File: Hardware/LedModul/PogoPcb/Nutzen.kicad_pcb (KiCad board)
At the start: 2 copper layers, 96 x 96 mm, 150 parts, among them J1 Conn_01x01_Pin, J2 Conn_01x01_Pin, J3 Conn_01x01_Pin, J4 Conn_01x01_Pin, J5 Conn_01x01_Pin, J6 Conn_01x01_Pin

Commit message: added gerber data
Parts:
- removed the J1 at (80.4, 98.5)
- removed the J1 at (99.6, 79.3)
- removed the J1 at (157.2, 79.3)
- removed the J1 at (138.0, 79.3)
- removed the J1 at (99.6, 60.1)
- removed the J1 at (138.0, 98.5)
- removed the J1 at (80.4, 79.3)
- removed the J1 at (118.8, 60.1)
- removed the J1 at (138.0, 136.9)
- removed the J1 at (99.6, 136.9)
- removed the J1 at (157.2, 60.1)
- removed the J1 at (99.6, 117.7)
- removed the J1 at (138.0, 60.1)
- removed the J1 at (118.8, 79.3)
- removed the J1 at (99.6, 98.5)
- removed the J1 at (80.4, 136.9)
- removed the J1 at (157.2, 117.7)
- removed the J1 at (138.0, 117.7)
- removed the J1 at (157.2, 136.9)
- removed the J1 at (80.4, 117.7)
- removed the J1 at (157.2, 98.5)
- removed the J1 at (118.8, 117.7)
- removed the J1 at (80.4, 60.1)
- removed the J1 at (118.8, 136.9)
- removed the J1 at (118.8, 98.5)
- removed the J2 at (102.8, 115.4)
- removed the J2 at (122.0, 115.4)
- removed the J2 at (83.6, 115.4)
- removed the J2 at (160.4, 134.6)
- removed the J2 at (160.4, 57.8)
- removed the J2 at (102.8, 96.2)
- removed the J2 at (102.8, 134.6)
- removed the J2 at (141.2, 134.6)
- removed the J2 at (141.2, 57.8)
- removed the J2 at (102.8, 57.8)
- removed the J2 at (141.2, 115.4)
- removed the J2 at (102.8, 77.0)
- removed the J2 at (122.0, 96.2)
- removed the J2 at (83.6, 77.0)
- removed the J2 at (141.2, 77.0)
- removed the J2 at (160.4, 96.2)
- removed the J2 at (122.0, 57.8)
- removed the J2 at (141.2, 96.2)
- removed the J2 at (122.0, 77.0)
- removed the J2 at (160.4, 115.4)
- removed the J2 at (122.0, 134.6)
- removed the J2 at (160.4, 77.0)
- removed the J2 at (83.6, 96.2)
- removed the J2 at (83.6, 134.6)
- removed the J2 at (83.6, 57.8)
- removed the J3 at (73.2, 77.0)
- removed the J3 at (73.2, 134.6)
- removed the J3 at (92.4, 77.0)
- removed the J3 at (92.4, 57.8)
- removed the J3 at (73.2, 57.8)
- removed the J3 at (150.0, 96.2)
- removed the J3 at (73.2, 96.2)
- removed the J3 at (130.8, 77.0)
- removed the J3 at (130.8, 57.8)
- removed the J3 at (111.6, 115.4)
- removed the J3 at (92.4, 96.2)
- removed the J3 at (111.6, 96.2)
- removed the J3 at (111.6, 134.6)
- removed the J3 at (130.8, 134.6)
- removed the J3 at (111.6, 57.8)
- removed the J3 at (150.0, 134.6)
- removed the J3 at (73.2, 115.4)
- removed the J3 at (150.0, 77.0)
- removed the J3 at (111.6, 77.0)
- removed the J3 at (150.0, 57.8)
- removed the J3 at (92.4, 134.6)
- removed the J3 at (92.4, 115.4)
- removed the J3 at (150.0, 115.4)
- removed the J3 at (130.8, 115.4)
- removed the J3 at (130.8, 96.2)
- removed the J4 at (134.0, 117.7)
- removed the J4 at (114.8, 98.5)
- removed the J4 at (114.8, 136.9)
- removed the J4 at (114.8, 117.7)
- removed the J4 at (76.4, 98.5)
- removed the J4 at (95.6, 98.5)
- removed the J4 at (76.4, 136.9)
- removed the J4 at (153.2, 60.1)
- removed the J4 at (114.8, 79.3)
- removed the J4 at (114.8, 60.1)
- removed the J4 at (76.4, 60.1)
- removed the J4 at (95.6, 136.9)
- removed the J4 at (134.0, 98.5)
- removed the J4 at (95.6, 79.3)
- removed the J4 at (134.0, 136.9)
- removed the J4 at (153.2, 98.5)
- removed the J4 at (95.6, 60.1)
- removed the J4 at (153.2, 136.9)
- removed the J4 at (134.0, 79.3)
- removed the J4 at (76.4, 79.3)
- removed the J4 at (95.6, 117.7)
- removed the J4 at (76.4, 117.7)
- removed the J4 at (134.0, 60.1)
- removed the J4 at (153.2, 117.7)
- removed the J4 at (153.2, 79.3)
- removed the J5 at (155.2, 68.0)
- removed the J5 at (78.4, 106.4)
- removed the J5 at (97.6, 87.2)
- removed the J5 at (78.4, 68.0)
- removed the J5 at (136.0, 87.2)
- removed the J5 at (136.0, 48.8)
- removed the J5 at (155.2, 125.6)
- removed the J5 at (116.8, 106.4)
- removed the J5 at (155.2, 48.8)
- removed the J5 at (116.8, 68.0)
- removed the J5 at (116.8, 125.6)
- removed the J5 at (97.6, 125.6)
- removed the J5 at (116.8, 87.2)
- removed the J5 at (136.0, 125.6)
- removed the J5 at (97.6, 106.4)
- removed the J5 at (78.4, 48.8)
- removed the J5 at (136.0, 68.0)
- removed the J5 at (78.4, 87.2)
- removed the J5 at (97.6, 68.0)
- removed the J5 at (155.2, 106.4)
- removed the J5 at (136.0, 106.4)
- removed the J5 at (155.2, 87.2)
- removed the J5 at (116.8, 48.8)
- removed the J5 at (97.6, 48.8)
- removed the J5 at (78.4, 125.6)
- removed the J6 at (97.6, 136.9)
- removed the J6 at (97.6, 60.1)
- removed the J6 at (116.8, 79.3)
- removed the J6 at (155.2, 117.7)
- removed the J6 at (78.4, 98.5)
- removed the J6 at (78.4, 79.3)
- removed the J6 at (78.4, 117.7)
- removed the J6 at (136.0, 79.3)
- removed the J6 at (97.6, 98.5)
- removed the J6 at (116.8, 98.5)
- removed the J6 at (155.2, 79.3)
- removed the J6 at (136.0, 136.9)
- removed the J6 at (136.0, 60.1)
- removed the J6 at (97.6, 117.7)
- removed the J6 at (78.4, 60.1)
- removed the J6 at (97.6, 79.3)
- removed the J6 at (155.2, 60.1)
- removed the J6 at (116.8, 117.7)
- removed the J6 at (155.2, 98.5)
- removed the J6 at (155.2, 136.9)
- removed the J6 at (78.4, 136.9)
- removed the J6 at (116.8, 136.9)
- removed the J6 at (136.0, 98.5)
- removed the J6 at (136.0, 117.7)
- removed the J6 at (116.8, 60.1)
- added J1: Conn_01x01_Pin, Bergi:Solderpad_1x2, B.Cu at (114.0, 88.8)
- added J1: Conn_01x01_Pin, Bergi:Solderpad_1x2, B.Cu at (190.8, 88.8)
- added J1: Conn_01x01_Pin, Bergi:Solderpad_1x2, B.Cu at (171.7, 108.0)
- added J1: Conn_01x01_Pin, Bergi:Solderpad_1x2, B.Cu at (133.2, 50.4)
- added J1: Conn_01x01_Pin, Bergi:Solderpad_1x2, B.Cu at (133.2, 127.2)
- added J1: Conn_01x01_Pin, Bergi:Solderpad_1x2, B.Cu at (190.8, 50.4)
- added J1: Conn_01x01_Pin, Bergi:Solderpad_1x2, B.Cu at (171.7, 50.4)
- added J1: Conn_01x01_Pin, Bergi:Solderpad_1x2, B.Cu at (152.4, 88.8)
- added J1: Conn_01x01_Pin, Bergi:Solderpad_1x2, B.Cu at (114.0, 69.6)
- added J1: Conn_01x01_Pin, Bergi:Solderpad_1x2, B.Cu at (190.8, 127.2)
- added J1: Conn_01x01_Pin, Bergi:Solderpad_1x2, B.Cu at (152.4, 127.2)
- added J1: Conn_01x01_Pin, Bergi:Solderpad_1x2, B.Cu at (133.2, 108.0)
- added J1: Conn_01x01_Pin, Bergi:Solderpad_1x2, B.Cu at (114.0, 127.2)
- added J1: Conn_01x01_Pin, Bergi:Solderpad_1x2, B.Cu at (114.0, 108.0)
- added J1: Conn_01x01_Pin, Bergi:Solderpad_1x2, B.Cu at (152.4, 50.4)
- added J1: Conn_01x01_Pin, Bergi:Solderpad_1x2, B.Cu at (133.2, 88.8)
- added J1: Conn_01x01_Pin, Bergi:Solderpad_1x2, B.Cu at (171.7, 127.2)
- added J1: Conn_01x01_Pin, Bergi:Solderpad_1x2, B.Cu at (152.4, 108.0)
- added J1: Conn_01x01_Pin, Bergi:Solderpad_1x2, B.Cu at (171.7, 88.8)
- added J1: Conn_01x01_Pin, Bergi:Solderpad_1x2, B.Cu at (171.7, 69.6)
- added J1: Conn_01x01_Pin, Bergi:Solderpad_1x2, B.Cu at (133.2, 69.6)
- added J1: Conn_01x01_Pin, Bergi:Solderpad_1x2, B.Cu at (114.0, 50.4)
- added J1: Conn_01x01_Pin, Bergi:Solderpad_1x2, B.Cu at (152.4, 69.6)
- added J1: Conn_01x01_Pin, Bergi:Solderpad_1x2, B.Cu at (190.8, 108.0)
- added J1: Conn_01x01_Pin, Bergi:Solderpad_1x2, B.Cu at (190.8, 69.6)
- added J2: Conn_01x01_Pin, TestPoint:TestPoint_Pad_D2.0mm, F.Cu at (136.4, 67.3)
- added J2: Conn_01x01_Pin, TestPoint:TestPoint_Pad_D2.0mm, F.Cu at (194.1, 48.1)
- added J2: Conn_01x01_Pin, TestPoint:TestPoint_Pad_D2.0mm, F.Cu at (194.1, 86.5)
- added J2: Conn_01x01_Pin, TestPoint:TestPoint_Pad_D2.0mm, F.Cu at (155.7, 48.1)
- added J2: Conn_01x01_Pin, TestPoint:TestPoint_Pad_D2.0mm, F.Cu at (117.2, 67.3)
- added J2: Conn_01x01_Pin, TestPoint:TestPoint_Pad_D2.0mm, F.Cu at (155.7, 86.5)
- added J2: Conn_01x01_Pin, TestPoint:TestPoint_Pad_D2.0mm, F.Cu at (174.8, 86.5)
- added J2: Conn_01x01_Pin, TestPoint:TestPoint_Pad_D2.0mm, F.Cu at (155.7, 105.7)
- added J2: Conn_01x01_Pin, TestPoint:TestPoint_Pad_D2.0mm, F.Cu at (155.7, 67.3)
- added J2: Conn_01x01_Pin, TestPoint:TestPoint_Pad_D2.0mm, F.Cu at (194.1, 105.7)
- added J2: Conn_01x01_Pin, TestPoint:TestPoint_Pad_D2.0mm, F.Cu at (117.2, 124.9)
- added J2: Conn_01x01_Pin, TestPoint:TestPoint_Pad_D2.0mm, F.Cu at (136.4, 86.5)
- added J2: Conn_01x01_Pin, TestPoint:TestPoint_Pad_D2.0mm, F.Cu at (117.2, 105.7)
- added J2: Conn_01x01_Pin, TestPoint:TestPoint_Pad_D2.0mm, F.Cu at (117.2, 48.1)
- added J2: Conn_01x01_Pin, TestPoint:TestPoint_Pad_D2.0mm, F.Cu at (194.1, 124.9)
- added J2: Conn_01x01_Pin, TestPoint:TestPoint_Pad_D2.0mm, F.Cu at (136.4, 48.1)
- added J2: Conn_01x01_Pin, TestPoint:TestPoint_Pad_D2.0mm, F.Cu at (174.8, 67.3)
- added J2: Conn_01x01_Pin, TestPoint:TestPoint_Pad_D2.0mm, F.Cu at (136.4, 124.9)
- added J2: Conn_01x01_Pin, TestPoint:TestPoint_Pad_D2.0mm, F.Cu at (117.2, 86.5)
- added J2: Conn_01x01_Pin, TestPoint:TestPoint_Pad_D2.0mm, F.Cu at (155.7, 124.9)
- added J2: Conn_01x01_Pin, TestPoint:TestPoint_Pad_D2.0mm, F.Cu at (174.8, 105.7)
- added J2: Conn_01x01_Pin, TestPoint:TestPoint_Pad_D2.0mm, F.Cu at (136.4, 105.7)
- added J2: Conn_01x01_Pin, TestPoint:TestPoint_Pad_D2.0mm, F.Cu at (174.8, 124.9)
- added J2: Conn_01x01_Pin, TestPoint:TestPoint_Pad_D2.0mm, F.Cu at (194.1, 67.3)
- added J2: Conn_01x01_Pin, TestPoint:TestPoint_Pad_D2.0mm, F.Cu at (174.8, 48.1)
- added J3: Conn_01x01_Pin, TestPoint:TestPoint_Pad_D2.0mm, F.Cu at (126.0, 48.1)
- added J3: Conn_01x01_Pin, TestPoint:TestPoint_Pad_D2.0mm, F.Cu at (126.0, 105.7)
- added J3: Conn_01x01_Pin, TestPoint:TestPoint_Pad_D2.0mm, F.Cu at (164.4, 86.5)
- added J3: Conn_01x01_Pin, TestPoint:TestPoint_Pad_D2.0mm, F.Cu at (183.7, 86.5)
- added J3: Conn_01x01_Pin, TestPoint:TestPoint_Pad_D2.0mm, F.Cu at (164.4, 48.1)
- added J3: Conn_01x01_Pin, TestPoint:TestPoint_Pad_D2.0mm, F.Cu at (164.4, 105.7)
- added J3: Conn_01x01_Pin, TestPoint:TestPoint_Pad_D2.0mm, F.Cu at (145.2, 124.9)
- added J3: Conn_01x01_Pin, TestPoint:TestPoint_Pad_D2.0mm, F.Cu at (183.7, 105.7)
- added J3: Conn_01x01_Pin, TestPoint:TestPoint_Pad_D2.0mm, F.Cu at (145.2, 105.7)
- added J3: Conn_01x01_Pin, TestPoint:TestPoint_Pad_D2.0mm, F.Cu at (126.0, 124.9)
- added J3: Conn_01x01_Pin, TestPoint:TestPoint_Pad_D2.0mm, F.Cu at (183.7, 124.9)
- added J3: Conn_01x01_Pin, TestPoint:TestPoint_Pad_D2.0mm, F.Cu at (183.7, 67.3)
- added J3: Conn_01x01_Pin, TestPoint:TestPoint_Pad_D2.0mm, F.Cu at (106.8, 124.9)
- added J3: Conn_01x01_Pin, TestPoint:TestPoint_Pad_D2.0mm, F.Cu at (145.2, 48.1)
- added J3: Conn_01x01_Pin, TestPoint:TestPoint_Pad_D2.0mm, F.Cu at (106.8, 48.1)
- added J3: Conn_01x01_Pin, TestPoint:TestPoint_Pad_D2.0mm, F.Cu at (145.2, 67.3)
- added J3: Conn_01x01_Pin, TestPoint:TestPoint_Pad_D2.0mm, F.Cu at (106.8, 86.5)
- added J3: Conn_01x01_Pin, TestPoint:TestPoint_Pad_D2.0mm, F.Cu at (106.8, 67.3)
- added J3: Conn_01x01_Pin, TestPoint:TestPoint_Pad_D2.0mm, F.Cu at (145.2, 86.5)
- added J3: Conn_01x01_Pin, TestPoint:TestPoint_Pad_D2.0mm, F.Cu at (164.4, 124.9)
- added J3: Conn_01x01_Pin, TestPoint:TestPoint_Pad_D2.0mm, F.Cu at (164.4, 67.3)
- added J3: Conn_01x01_Pin, TestPoint:TestPoint_Pad_D2.0mm, F.Cu at (183.7, 48.1)
- added J3: Conn_01x01_Pin, TestPoint:TestPoint_Pad_D2.0mm, F.Cu at (126.0, 86.5)
- added J3: Conn_01x01_Pin, TestPoint:TestPoint_Pad_D2.0mm, F.Cu at (126.0, 67.3)
- added J3: Conn_01x01_Pin, TestPoint:TestPoint_Pad_D2.0mm, F.Cu at (106.8, 105.7)
- added J4: Conn_01x01_Pin, Bergi:Solderpad_1x2, B.Cu at (167.7, 108.0)
- added J4: Conn_01x01_Pin, Bergi:Solderpad_1x2, B.Cu at (167.7, 127.2)
- added J4: Conn_01x01_Pin, Bergi:Solderpad_1x2, B.Cu at (110.0, 108.0)
- added J4: Conn_01x01_Pin, Bergi:Solderpad_1x2, B.Cu at (148.4, 88.8)
- added J4: Conn_01x01_Pin, Bergi:Solderpad_1x2, B.Cu at (186.8, 88.8)
- added J4: Conn_01x01_Pin, Bergi:Solderpad_1x2, B.Cu at (186.8, 108.0)
- added J4: Conn_01x01_Pin, Bergi:Solderpad_1x2, B.Cu at (129.2, 50.4)
- added J4: Conn_01x01_Pin, Bergi:Solderpad_1x2, B.Cu at (129.2, 127.2)
- added J4: Conn_01x01_Pin, Bergi:Solderpad_1x2, B.Cu at (129.2, 69.6)
- added J4: Conn_01x01_Pin, Bergi:Solderpad_1x2, B.Cu at (129.2, 108.0)
- added J4: Conn_01x01_Pin, Bergi:Solderpad_1x2, B.Cu at (148.4, 50.4)
- added J4: Conn_01x01_Pin, Bergi:Solderpad_1x2, B.Cu at (167.7, 88.8)
- added J4: Conn_01x01_Pin, Bergi:Solderpad_1x2, B.Cu at (167.7, 69.6)
- added J4: Conn_01x01_Pin, Bergi:Solderpad_1x2, B.Cu at (129.2, 88.8)
- added J4: Conn_01x01_Pin, Bergi:Solderpad_1x2, B.Cu at (110.0, 88.8)
- added J4: Conn_01x01_Pin, Bergi:Solderpad_1x2, B.Cu at (186.8, 50.4)
- added J4: Conn_01x01_Pin, Bergi:Solderpad_1x2, B.Cu at (186.8, 69.6)
- added J4: Conn_01x01_Pin, Bergi:Solderpad_1x2, B.Cu at (167.7, 50.4)
- added J4: Conn_01x01_Pin, Bergi:Solderpad_1x2, B.Cu at (148.4, 108.0)
- added J4: Conn_01x01_Pin, Bergi:Solderpad_1x2, B.Cu at (110.0, 127.2)
- added J4: Conn_01x01_Pin, Bergi:Solderpad_1x2, B.Cu at (148.4, 127.2)
- added J4: Conn_01x01_Pin, Bergi:Solderpad_1x2, B.Cu at (186.8, 127.2)
- added J4: Conn_01x01_Pin, Bergi:Solderpad_1x2, B.Cu at (110.0, 50.4)
- added J4: Conn_01x01_Pin, Bergi:Solderpad_1x2, B.Cu at (110.0, 69.6)
- added J4: Conn_01x01_Pin, Bergi:Solderpad_1x2, B.Cu at (148.4, 69.6)
- added J5: Conn_01x01_Pin, TestPoint:TestPoint_Pad_D2.0mm, F.Cu at (131.2, 115.9)
- added J5: Conn_01x01_Pin, TestPoint:TestPoint_Pad_D2.0mm, F.Cu at (112.0, 96.7)
- added J5: Conn_01x01_Pin, TestPoint:TestPoint_Pad_D2.0mm, F.Cu at (112.0, 58.3)
- added J5: Conn_01x01_Pin, TestPoint:TestPoint_Pad_D2.0mm, F.Cu at (112.0, 39.1)
- added J5: Conn_01x01_Pin, TestPoint:TestPoint_Pad_D2.0mm, F.Cu at (131.2, 77.5)
- added J5: Conn_01x01_Pin, TestPoint:TestPoint_Pad_D2.0mm, F.Cu at (188.8, 96.7)
- added J5: Conn_01x01_Pin, TestPoint:TestPoint_Pad_D2.0mm, F.Cu at (169.7, 115.9)
- added J5: Conn_01x01_Pin, TestPoint:TestPoint_Pad_D2.0mm, F.Cu at (169.7, 39.1)
- added J5: Conn_01x01_Pin, TestPoint:TestPoint_Pad_D2.0mm, F.Cu at (150.4, 96.7)
- added J5: Conn_01x01_Pin, TestPoint:TestPoint_Pad_D2.0mm, F.Cu at (112.0, 115.9)
- added J5: Conn_01x01_Pin, TestPoint:TestPoint_Pad_D2.0mm, F.Cu at (112.0, 77.5)
- added J5: Conn_01x01_Pin, TestPoint:TestPoint_Pad_D2.0mm, F.Cu at (131.2, 58.3)
- added J5: Conn_01x01_Pin, TestPoint:TestPoint_Pad_D2.0mm, F.Cu at (188.8, 115.9)
- added J5: Conn_01x01_Pin, TestPoint:TestPoint_Pad_D2.0mm, F.Cu at (131.2, 96.7)
- added J5: Conn_01x01_Pin, TestPoint:TestPoint_Pad_D2.0mm, F.Cu at (169.7, 58.3)
- added J5: Conn_01x01_Pin, TestPoint:TestPoint_Pad_D2.0mm, F.Cu at (169.7, 77.5)
- added J5: Conn_01x01_Pin, TestPoint:TestPoint_Pad_D2.0mm, F.Cu at (188.8, 77.5)
- added J5: Conn_01x01_Pin, TestPoint:TestPoint_Pad_D2.0mm, F.Cu at (150.4, 77.5)
- added J5: Conn_01x01_Pin, TestPoint:TestPoint_Pad_D2.0mm, F.Cu at (188.8, 39.1)
- added J5: Conn_01x01_Pin, TestPoint:TestPoint_Pad_D2.0mm, F.Cu at (131.2, 39.1)
- added J5: Conn_01x01_Pin, TestPoint:TestPoint_Pad_D2.0mm, F.Cu at (169.7, 96.7)
- added J5: Conn_01x01_Pin, TestPoint:TestPoint_Pad_D2.0mm, F.Cu at (188.8, 58.3)
- added J5: Conn_01x01_Pin, TestPoint:TestPoint_Pad_D2.0mm, F.Cu at (150.4, 115.9)
- added J5: Conn_01x01_Pin, TestPoint:TestPoint_Pad_D2.0mm, F.Cu at (150.4, 39.1)
- added J5: Conn_01x01_Pin, TestPoint:TestPoint_Pad_D2.0mm, F.Cu at (150.4, 58.3)
- added J6: Conn_01x01_Pin, Bergi:Solderpad_1x2, B.Cu at (169.7, 127.2)
- added J6: Conn_01x01_Pin, Bergi:Solderpad_1x2, B.Cu at (131.2, 127.2)
- added J6: Conn_01x01_Pin, Bergi:Solderpad_1x2, B.Cu at (112.0, 69.6)
- added J6: Conn_01x01_Pin, Bergi:Solderpad_1x2, B.Cu at (131.2, 88.8)
- added J6: Conn_01x01_Pin, Bergi:Solderpad_1x2, B.Cu at (188.8, 88.8)
- added J6: Conn_01x01_Pin, Bergi:Solderpad_1x2, B.Cu at (150.4, 50.4)
- added J6: Conn_01x01_Pin, Bergi:Solderpad_1x2, B.Cu at (131.2, 50.4)
- added J6: Conn_01x01_Pin, Bergi:Solderpad_1x2, B.Cu at (150.4, 108.0)
- added J6: Conn_01x01_Pin, Bergi:Solderpad_1x2, B.Cu at (112.0, 108.0)
- added J6: Conn_01x01_Pin, Bergi:Solderpad_1x2, B.Cu at (169.7, 50.4)
- added J6: Conn_01x01_Pin, Bergi:Solderpad_1x2, B.Cu at (150.4, 88.8)
- added J6: Conn_01x01_Pin, Bergi:Solderpad_1x2, B.Cu at (150.4, 127.2)
- added J6: Conn_01x01_Pin, Bergi:Solderpad_1x2, B.Cu at (169.7, 69.6)
- added J6: Conn_01x01_Pin, Bergi:Solderpad_1x2, B.Cu at (112.0, 127.2)
- added J6: Conn_01x01_Pin, Bergi:Solderpad_1x2, B.Cu at (169.7, 108.0)
- added J6: Conn_01x01_Pin, Bergi:Solderpad_1x2, B.Cu at (131.2, 108.0)
- added J6: Conn_01x01_Pin, Bergi:Solderpad_1x2, B.Cu at (188.8, 108.0)
- added J6: Conn_01x01_Pin, Bergi:Solderpad_1x2, B.Cu at (150.4, 69.6)
- added J6: Conn_01x01_Pin, Bergi:Solderpad_1x2, B.Cu at (112.0, 50.4)
- added J6: Conn_01x01_Pin, Bergi:Solderpad_1x2, B.Cu at (188.8, 69.6)
- added J6: Conn_01x01_Pin, Bergi:Solderpad_1x2, B.Cu at (169.7, 88.8)
- added J6: Conn_01x01_Pin, Bergi:Solderpad_1x2, B.Cu at (112.0, 88.8)
- added J6: Conn_01x01_Pin, Bergi:Solderpad_1x2, B.Cu at (188.8, 127.2)
- added J6: Conn_01x01_Pin, Bergi:Solderpad_1x2, B.Cu at (131.2, 69.6)
- added J6: Conn_01x01_Pin, Bergi:Solderpad_1x2, B.Cu at (188.8, 50.4)

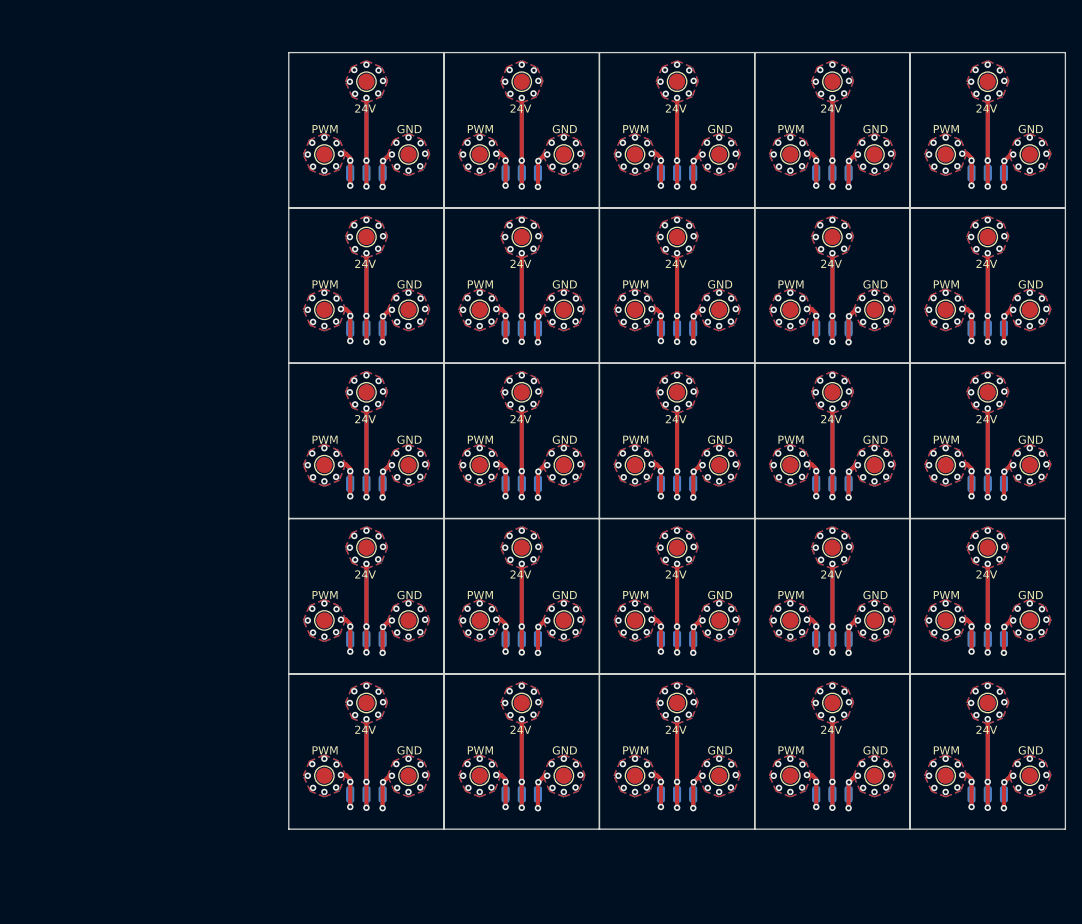
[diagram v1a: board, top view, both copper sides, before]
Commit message: added Pcb name and version to silkscreen
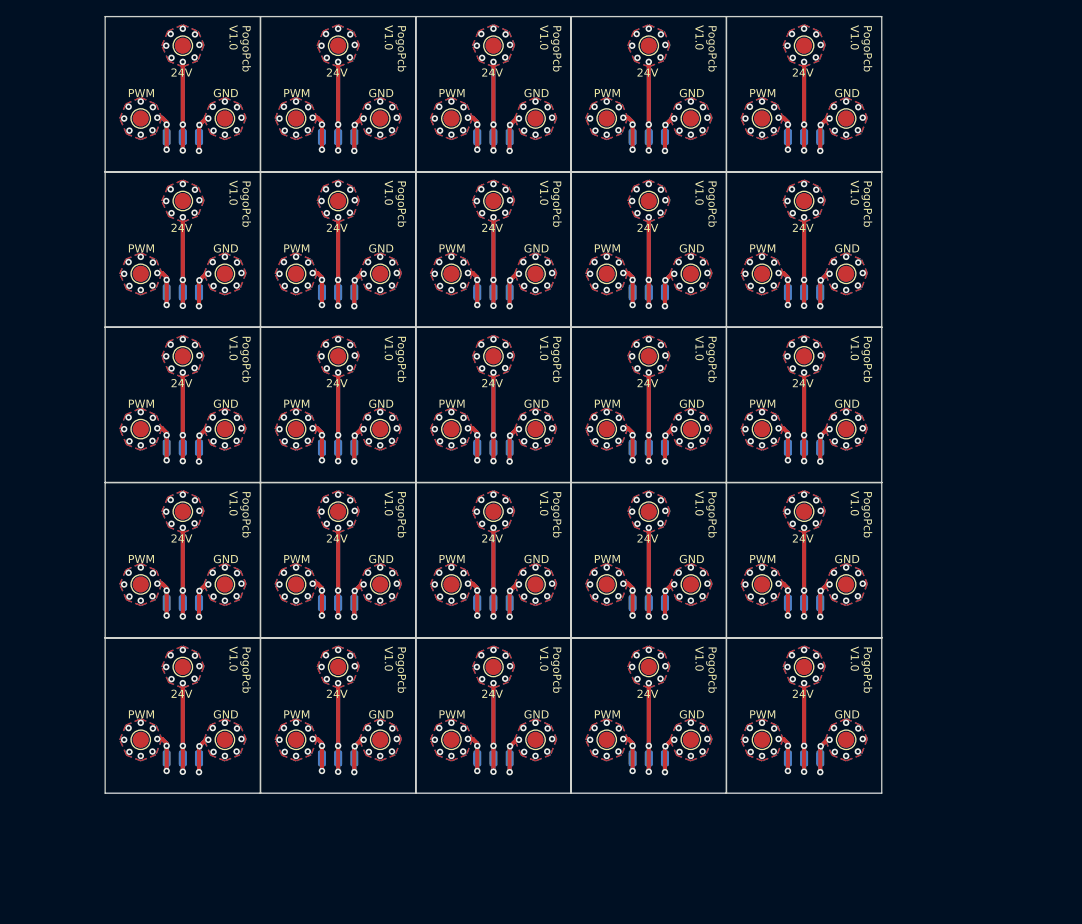
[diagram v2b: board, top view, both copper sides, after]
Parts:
- removed the J1 at (114.0, 88.8)
- removed the J1 at (190.8, 88.8)
- removed the J1 at (171.7, 108.0)
- removed the J1 at (133.2, 50.4)
- removed the J1 at (133.2, 127.2)
- removed the J1 at (190.8, 50.4)
- removed the J1 at (171.7, 50.4)
- removed the J1 at (152.4, 88.8)
- removed the J1 at (114.0, 69.6)
- removed the J1 at (190.8, 127.2)
- removed the J1 at (152.4, 127.2)
- removed the J1 at (133.2, 108.0)
- removed the J1 at (114.0, 127.2)
- removed the J1 at (114.0, 108.0)
- removed the J1 at (152.4, 50.4)
- removed the J1 at (133.2, 88.8)
- removed the J1 at (171.7, 127.2)
- removed the J1 at (152.4, 108.0)
- removed the J1 at (171.7, 88.8)
- removed the J1 at (171.7, 69.6)
- removed the J1 at (133.2, 69.6)
- removed the J1 at (114.0, 50.4)
- removed the J1 at (152.4, 69.6)
- removed the J1 at (190.8, 108.0)
- removed the J1 at (190.8, 69.6)
- removed the J2 at (136.4, 67.3)
- removed the J2 at (194.1, 48.1)
- removed the J2 at (194.1, 86.5)
- removed the J2 at (155.7, 48.1)
- removed the J2 at (117.2, 67.3)
- removed the J2 at (155.7, 86.5)
- removed the J2 at (174.8, 86.5)
- removed the J2 at (155.7, 105.7)
- removed the J2 at (155.7, 67.3)
- removed the J2 at (194.1, 105.7)
- removed the J2 at (117.2, 124.9)
- removed the J2 at (136.4, 86.5)
- removed the J2 at (117.2, 105.7)
- removed the J2 at (117.2, 48.1)
- removed the J2 at (194.1, 124.9)
- removed the J2 at (136.4, 48.1)
- removed the J2 at (174.8, 67.3)
- removed the J2 at (136.4, 124.9)
- removed the J2 at (117.2, 86.5)
- removed the J2 at (155.7, 124.9)
- removed the J2 at (174.8, 105.7)
- removed the J2 at (136.4, 105.7)
- removed the J2 at (174.8, 124.9)
- removed the J2 at (194.1, 67.3)
- removed the J2 at (174.8, 48.1)
- removed the J3 at (126.0, 48.1)
- removed the J3 at (126.0, 105.7)
- removed the J3 at (164.4, 86.5)
- removed the J3 at (183.7, 86.5)
- removed the J3 at (164.4, 48.1)
- removed the J3 at (164.4, 105.7)
- removed the J3 at (145.2, 124.9)
- removed the J3 at (183.7, 105.7)
- removed the J3 at (145.2, 105.7)
- removed the J3 at (126.0, 124.9)
- removed the J3 at (183.7, 124.9)
- removed the J3 at (183.7, 67.3)
- removed the J3 at (106.8, 124.9)
- removed the J3 at (145.2, 48.1)
- removed the J3 at (106.8, 48.1)
- removed the J3 at (145.2, 67.3)
- removed the J3 at (106.8, 86.5)
- removed the J3 at (106.8, 67.3)
- removed the J3 at (145.2, 86.5)
- removed the J3 at (164.4, 124.9)
- removed the J3 at (164.4, 67.3)
- removed the J3 at (183.7, 48.1)
- removed the J3 at (126.0, 86.5)
- removed the J3 at (126.0, 67.3)
- removed the J3 at (106.8, 105.7)
- removed the J4 at (167.7, 108.0)
- removed the J4 at (167.7, 127.2)
- removed the J4 at (110.0, 108.0)
- removed the J4 at (148.4, 88.8)
- removed the J4 at (186.8, 88.8)
- removed the J4 at (186.8, 108.0)
- removed the J4 at (129.2, 50.4)
- removed the J4 at (129.2, 127.2)
- removed the J4 at (129.2, 69.6)
- removed the J4 at (129.2, 108.0)
- removed the J4 at (148.4, 50.4)
- removed the J4 at (167.7, 88.8)
- removed the J4 at (167.7, 69.6)
- removed the J4 at (129.2, 88.8)
- removed the J4 at (110.0, 88.8)
- removed the J4 at (186.8, 50.4)
- removed the J4 at (186.8, 69.6)
- removed the J4 at (167.7, 50.4)
- removed the J4 at (148.4, 108.0)
- removed the J4 at (110.0, 127.2)
- removed the J4 at (148.4, 127.2)
- removed the J4 at (186.8, 127.2)
- removed the J4 at (110.0, 50.4)
- removed the J4 at (110.0, 69.6)
- removed the J4 at (148.4, 69.6)
- removed the J5 at (131.2, 115.9)
- removed the J5 at (112.0, 96.7)
- removed the J5 at (112.0, 58.3)
- removed the J5 at (112.0, 39.1)
- removed the J5 at (131.2, 77.5)
- removed the J5 at (188.8, 96.7)
- removed the J5 at (169.7, 115.9)
- removed the J5 at (169.7, 39.1)
- removed the J5 at (150.4, 96.7)
- removed the J5 at (112.0, 115.9)
- removed the J5 at (112.0, 77.5)
- removed the J5 at (131.2, 58.3)
- removed the J5 at (188.8, 115.9)
- removed the J5 at (131.2, 96.7)
- removed the J5 at (169.7, 58.3)
- removed the J5 at (169.7, 77.5)
- removed the J5 at (188.8, 77.5)
- removed the J5 at (150.4, 77.5)
- removed the J5 at (188.8, 39.1)
- removed the J5 at (131.2, 39.1)
- removed the J5 at (169.7, 96.7)
- removed the J5 at (188.8, 58.3)
- removed the J5 at (150.4, 115.9)
- removed the J5 at (150.4, 39.1)
- removed the J5 at (150.4, 58.3)
- removed the J6 at (169.7, 127.2)
- removed the J6 at (131.2, 127.2)
- removed the J6 at (112.0, 69.6)
- removed the J6 at (131.2, 88.8)
- removed the J6 at (188.8, 88.8)
- removed the J6 at (150.4, 50.4)
- removed the J6 at (131.2, 50.4)
- removed the J6 at (150.4, 108.0)
- removed the J6 at (112.0, 108.0)
- removed the J6 at (169.7, 50.4)
- removed the J6 at (150.4, 88.8)
- removed the J6 at (150.4, 127.2)
- removed the J6 at (169.7, 69.6)
- removed the J6 at (112.0, 127.2)
- removed the J6 at (169.7, 108.0)
- removed the J6 at (131.2, 108.0)
- removed the J6 at (188.8, 108.0)
- removed the J6 at (150.4, 69.6)
- removed the J6 at (112.0, 50.4)
- removed the J6 at (188.8, 69.6)
- removed the J6 at (169.7, 88.8)
- removed the J6 at (112.0, 88.8)
- removed the J6 at (188.8, 127.2)
- removed the J6 at (131.2, 69.6)
- removed the J6 at (188.8, 50.4)
- added J1: Conn_01x01_Pin, Bergi:Solderpad_1x2, B.Cu at (110.5, 65.2)
- added J1: Conn_01x01_Pin, Bergi:Solderpad_1x2, B.Cu at (110.5, 84.3)
- added J1: Conn_01x01_Pin, Bergi:Solderpad_1x2, B.Cu at (148.9, 122.8)
- added J1: Conn_01x01_Pin, Bergi:Solderpad_1x2, B.Cu at (91.3, 65.2)
- added J1: Conn_01x01_Pin, Bergi:Solderpad_1x2, B.Cu at (129.8, 65.2)
- added J1: Conn_01x01_Pin, Bergi:Solderpad_1x2, B.Cu at (129.8, 46.0)
- added J1: Conn_01x01_Pin, Bergi:Solderpad_1x2, B.Cu at (110.5, 46.0)
- added J1: Conn_01x01_Pin, Bergi:Solderpad_1x2, B.Cu at (129.8, 103.5)
- added J1: Conn_01x01_Pin, Bergi:Solderpad_1x2, B.Cu at (91.3, 84.3)
- added J1: Conn_01x01_Pin, Bergi:Solderpad_1x2, B.Cu at (148.9, 84.3)
- added J1: Conn_01x01_Pin, Bergi:Solderpad_1x2, B.Cu at (148.9, 103.5)
- added J1: Conn_01x01_Pin, Bergi:Solderpad_1x2, B.Cu at (129.8, 84.3)
- added J1: Conn_01x01_Pin, Bergi:Solderpad_1x2, B.Cu at (91.3, 103.5)
- added J1: Conn_01x01_Pin, Bergi:Solderpad_1x2, B.Cu at (168.2, 65.2)
- added J1: Conn_01x01_Pin, Bergi:Solderpad_1x2, B.Cu at (110.5, 122.8)
- added J1: Conn_01x01_Pin, Bergi:Solderpad_1x2, B.Cu at (168.2, 84.3)
- added J1: Conn_01x01_Pin, Bergi:Solderpad_1x2, B.Cu at (168.2, 103.5)
- added J1: Conn_01x01_Pin, Bergi:Solderpad_1x2, B.Cu at (168.2, 122.8)
- added J1: Conn_01x01_Pin, Bergi:Solderpad_1x2, B.Cu at (91.3, 46.0)
- added J1: Conn_01x01_Pin, Bergi:Solderpad_1x2, B.Cu at (91.3, 122.8)
- added J1: Conn_01x01_Pin, Bergi:Solderpad_1x2, B.Cu at (168.2, 46.0)
- added J1: Conn_01x01_Pin, Bergi:Solderpad_1x2, B.Cu at (148.9, 65.2)
- added J1: Conn_01x01_Pin, Bergi:Solderpad_1x2, B.Cu at (129.8, 122.8)
- added J1: Conn_01x01_Pin, Bergi:Solderpad_1x2, B.Cu at (110.5, 103.5)
- added J1: Conn_01x01_Pin, Bergi:Solderpad_1x2, B.Cu at (148.9, 46.0)
- added J2: Conn_01x01_Pin, TestPoint:TestPoint_Pad_D2.0mm, F.Cu at (152.2, 82.0)
- added J2: Conn_01x01_Pin, TestPoint:TestPoint_Pad_D2.0mm, F.Cu at (132.9, 43.6)
- added J2: Conn_01x01_Pin, TestPoint:TestPoint_Pad_D2.0mm, F.Cu at (113.8, 120.5)
- added J2: Conn_01x01_Pin, TestPoint:TestPoint_Pad_D2.0mm, F.Cu at (132.9, 120.5)
- added J2: Conn_01x01_Pin, TestPoint:TestPoint_Pad_D2.0mm, F.Cu at (94.5, 120.5)
- added J2: Conn_01x01_Pin, TestPoint:TestPoint_Pad_D2.0mm, F.Cu at (171.3, 62.9)
- added J2: Conn_01x01_Pin, TestPoint:TestPoint_Pad_D2.0mm, F.Cu at (152.2, 43.6)
- added J2: Conn_01x01_Pin, TestPoint:TestPoint_Pad_D2.0mm, F.Cu at (94.5, 62.9)
- added J2: Conn_01x01_Pin, TestPoint:TestPoint_Pad_D2.0mm, F.Cu at (113.8, 62.9)
- added J2: Conn_01x01_Pin, TestPoint:TestPoint_Pad_D2.0mm, F.Cu at (94.5, 82.0)
- added J2: Conn_01x01_Pin, TestPoint:TestPoint_Pad_D2.0mm, F.Cu at (132.9, 101.2)
- added J2: Conn_01x01_Pin, TestPoint:TestPoint_Pad_D2.0mm, F.Cu at (171.3, 101.2)
- added J2: Conn_01x01_Pin, TestPoint:TestPoint_Pad_D2.0mm, F.Cu at (113.8, 101.2)
- added J2: Conn_01x01_Pin, TestPoint:TestPoint_Pad_D2.0mm, F.Cu at (113.8, 43.6)
- added J2: Conn_01x01_Pin, TestPoint:TestPoint_Pad_D2.0mm, F.Cu at (113.8, 82.0)
- added J2: Conn_01x01_Pin, TestPoint:TestPoint_Pad_D2.0mm, F.Cu at (152.2, 62.9)
- added J2: Conn_01x01_Pin, TestPoint:TestPoint_Pad_D2.0mm, F.Cu at (132.9, 82.0)
- added J2: Conn_01x01_Pin, TestPoint:TestPoint_Pad_D2.0mm, F.Cu at (94.5, 43.6)
- added J2: Conn_01x01_Pin, TestPoint:TestPoint_Pad_D2.0mm, F.Cu at (171.3, 82.0)
- added J2: Conn_01x01_Pin, TestPoint:TestPoint_Pad_D2.0mm, F.Cu at (152.2, 120.5)
- added J2: Conn_01x01_Pin, TestPoint:TestPoint_Pad_D2.0mm, F.Cu at (152.2, 101.2)
- added J2: Conn_01x01_Pin, TestPoint:TestPoint_Pad_D2.0mm, F.Cu at (132.9, 62.9)
- added J2: Conn_01x01_Pin, TestPoint:TestPoint_Pad_D2.0mm, F.Cu at (171.3, 43.6)
- added J2: Conn_01x01_Pin, TestPoint:TestPoint_Pad_D2.0mm, F.Cu at (94.5, 101.2)
- added J2: Conn_01x01_Pin, TestPoint:TestPoint_Pad_D2.0mm, F.Cu at (171.3, 120.5)
- added J3: Conn_01x01_Pin, TestPoint:TestPoint_Pad_D2.0mm, F.Cu at (103.3, 82.0)
- added J3: Conn_01x01_Pin, TestPoint:TestPoint_Pad_D2.0mm, F.Cu at (122.5, 82.0)
- added J3: Conn_01x01_Pin, TestPoint:TestPoint_Pad_D2.0mm, F.Cu at (122.5, 62.9)
- added J3: Conn_01x01_Pin, TestPoint:TestPoint_Pad_D2.0mm, F.Cu at (122.5, 43.6)
- added J3: Conn_01x01_Pin, TestPoint:TestPoint_Pad_D2.0mm, F.Cu at (141.8, 62.9)
- added J3: Conn_01x01_Pin, TestPoint:TestPoint_Pad_D2.0mm, F.Cu at (84.2, 62.9)
- added J3: Conn_01x01_Pin, TestPoint:TestPoint_Pad_D2.0mm, F.Cu at (141.8, 43.6)
- added J3: Conn_01x01_Pin, TestPoint:TestPoint_Pad_D2.0mm, F.Cu at (103.3, 43.6)
- added J3: Conn_01x01_Pin, TestPoint:TestPoint_Pad_D2.0mm, F.Cu at (160.9, 43.6)
- added J3: Conn_01x01_Pin, TestPoint:TestPoint_Pad_D2.0mm, F.Cu at (141.8, 120.5)
- added J3: Conn_01x01_Pin, TestPoint:TestPoint_Pad_D2.0mm, F.Cu at (122.5, 120.5)
- added J3: Conn_01x01_Pin, TestPoint:TestPoint_Pad_D2.0mm, F.Cu at (84.2, 120.5)
- added J3: Conn_01x01_Pin, TestPoint:TestPoint_Pad_D2.0mm, F.Cu at (160.9, 120.5)
- added J3: Conn_01x01_Pin, TestPoint:TestPoint_Pad_D2.0mm, F.Cu at (160.9, 101.2)
- added J3: Conn_01x01_Pin, TestPoint:TestPoint_Pad_D2.0mm, F.Cu at (84.2, 101.2)
- added J3: Conn_01x01_Pin, TestPoint:TestPoint_Pad_D2.0mm, F.Cu at (141.8, 101.2)
- added J3: Conn_01x01_Pin, TestPoint:TestPoint_Pad_D2.0mm, F.Cu at (103.3, 101.2)
- added J3: Conn_01x01_Pin, TestPoint:TestPoint_Pad_D2.0mm, F.Cu at (141.8, 82.0)
- added J3: Conn_01x01_Pin, TestPoint:TestPoint_Pad_D2.0mm, F.Cu at (103.3, 120.5)
- added J3: Conn_01x01_Pin, TestPoint:TestPoint_Pad_D2.0mm, F.Cu at (160.9, 82.0)
- added J3: Conn_01x01_Pin, TestPoint:TestPoint_Pad_D2.0mm, F.Cu at (103.3, 62.9)
- added J3: Conn_01x01_Pin, TestPoint:TestPoint_Pad_D2.0mm, F.Cu at (160.9, 62.9)
- added J3: Conn_01x01_Pin, TestPoint:TestPoint_Pad_D2.0mm, F.Cu at (84.2, 43.6)
- added J3: Conn_01x01_Pin, TestPoint:TestPoint_Pad_D2.0mm, F.Cu at (122.5, 101.2)
- added J3: Conn_01x01_Pin, TestPoint:TestPoint_Pad_D2.0mm, F.Cu at (84.2, 82.0)
- added J4: Conn_01x01_Pin, Bergi:Solderpad_1x2, B.Cu at (144.9, 103.5)
- added J4: Conn_01x01_Pin, Bergi:Solderpad_1x2, B.Cu at (164.2, 46.0)
- added J4: Conn_01x01_Pin, Bergi:Solderpad_1x2, B.Cu at (164.2, 103.5)
- added J4: Conn_01x01_Pin, Bergi:Solderpad_1x2, B.Cu at (106.5, 65.2)
- added J4: Conn_01x01_Pin, Bergi:Solderpad_1x2, B.Cu at (106.5, 103.5)
- added J4: Conn_01x01_Pin, Bergi:Solderpad_1x2, B.Cu at (106.5, 46.0)
- added J4: Conn_01x01_Pin, Bergi:Solderpad_1x2, B.Cu at (87.3, 122.8)
- added J4: Conn_01x01_Pin, Bergi:Solderpad_1x2, B.Cu at (125.8, 65.2)
- added J4: Conn_01x01_Pin, Bergi:Solderpad_1x2, B.Cu at (106.5, 84.3)
- added J4: Conn_01x01_Pin, Bergi:Solderpad_1x2, B.Cu at (87.3, 46.0)
- added J4: Conn_01x01_Pin, Bergi:Solderpad_1x2, B.Cu at (125.8, 103.5)
- added J4: Conn_01x01_Pin, Bergi:Solderpad_1x2, B.Cu at (144.9, 122.8)
- added J4: Conn_01x01_Pin, Bergi:Solderpad_1x2, B.Cu at (87.3, 65.2)
- added J4: Conn_01x01_Pin, Bergi:Solderpad_1x2, B.Cu at (144.9, 46.0)
- added J4: Conn_01x01_Pin, Bergi:Solderpad_1x2, B.Cu at (125.8, 84.3)
- added J4: Conn_01x01_Pin, Bergi:Solderpad_1x2, B.Cu at (144.9, 84.3)
- added J4: Conn_01x01_Pin, Bergi:Solderpad_1x2, B.Cu at (125.8, 46.0)
- added J4: Conn_01x01_Pin, Bergi:Solderpad_1x2, B.Cu at (106.5, 122.8)
- added J4: Conn_01x01_Pin, Bergi:Solderpad_1x2, B.Cu at (164.2, 65.2)
- added J4: Conn_01x01_Pin, Bergi:Solderpad_1x2, B.Cu at (125.8, 122.8)
- added J4: Conn_01x01_Pin, Bergi:Solderpad_1x2, B.Cu at (144.9, 65.2)
- added J4: Conn_01x01_Pin, Bergi:Solderpad_1x2, B.Cu at (87.3, 84.3)
- added J4: Conn_01x01_Pin, Bergi:Solderpad_1x2, B.Cu at (164.2, 84.3)
- added J4: Conn_01x01_Pin, Bergi:Solderpad_1x2, B.Cu at (164.2, 122.8)
- added J4: Conn_01x01_Pin, Bergi:Solderpad_1x2, B.Cu at (87.3, 103.5)
- added J5: Conn_01x01_Pin, TestPoint:TestPoint_Pad_D2.0mm, F.Cu at (146.9, 73.0)
- added J5: Conn_01x01_Pin, TestPoint:TestPoint_Pad_D2.0mm, F.Cu at (108.5, 73.0)
- added J5: Conn_01x01_Pin, TestPoint:TestPoint_Pad_D2.0mm, F.Cu at (146.9, 34.6)
- added J5: Conn_01x01_Pin, TestPoint:TestPoint_Pad_D2.0mm, F.Cu at (127.8, 53.9)
- added J5: Conn_01x01_Pin, TestPoint:TestPoint_Pad_D2.0mm, F.Cu at (89.3, 111.5)
- added J5: Conn_01x01_Pin, TestPoint:TestPoint_Pad_D2.0mm, F.Cu at (89.3, 92.2)
- added J5: Conn_01x01_Pin, TestPoint:TestPoint_Pad_D2.0mm, F.Cu at (89.3, 73.0)
- added J5: Conn_01x01_Pin, TestPoint:TestPoint_Pad_D2.0mm, F.Cu at (89.3, 34.6)
- added J5: Conn_01x01_Pin, TestPoint:TestPoint_Pad_D2.0mm, F.Cu at (127.8, 111.5)
- added J5: Conn_01x01_Pin, TestPoint:TestPoint_Pad_D2.0mm, F.Cu at (166.2, 111.5)
- added J5: Conn_01x01_Pin, TestPoint:TestPoint_Pad_D2.0mm, F.Cu at (166.2, 34.6)
- added J5: Conn_01x01_Pin, TestPoint:TestPoint_Pad_D2.0mm, F.Cu at (108.5, 92.2)
- added J5: Conn_01x01_Pin, TestPoint:TestPoint_Pad_D2.0mm, F.Cu at (108.5, 53.9)
- added J5: Conn_01x01_Pin, TestPoint:TestPoint_Pad_D2.0mm, F.Cu at (108.5, 111.5)
- added J5: Conn_01x01_Pin, TestPoint:TestPoint_Pad_D2.0mm, F.Cu at (166.2, 73.0)
- added J5: Conn_01x01_Pin, TestPoint:TestPoint_Pad_D2.0mm, F.Cu at (146.9, 53.9)
- added J5: Conn_01x01_Pin, TestPoint:TestPoint_Pad_D2.0mm, F.Cu at (146.9, 111.5)
- added J5: Conn_01x01_Pin, TestPoint:TestPoint_Pad_D2.0mm, F.Cu at (108.5, 34.6)
- added J5: Conn_01x01_Pin, TestPoint:TestPoint_Pad_D2.0mm, F.Cu at (127.8, 34.6)
- added J5: Conn_01x01_Pin, TestPoint:TestPoint_Pad_D2.0mm, F.Cu at (166.2, 92.2)
- added J5: Conn_01x01_Pin, TestPoint:TestPoint_Pad_D2.0mm, F.Cu at (127.8, 73.0)
- added J5: Conn_01x01_Pin, TestPoint:TestPoint_Pad_D2.0mm, F.Cu at (166.2, 53.9)
- added J5: Conn_01x01_Pin, TestPoint:TestPoint_Pad_D2.0mm, F.Cu at (89.3, 53.9)
- added J5: Conn_01x01_Pin, TestPoint:TestPoint_Pad_D2.0mm, F.Cu at (146.9, 92.2)
- added J5: Conn_01x01_Pin, TestPoint:TestPoint_Pad_D2.0mm, F.Cu at (127.8, 92.2)
- added J6: Conn_01x01_Pin, Bergi:Solderpad_1x2, B.Cu at (89.3, 122.8)
- added J6: Conn_01x01_Pin, Bergi:Solderpad_1x2, B.Cu at (127.8, 65.2)
- added J6: Conn_01x01_Pin, Bergi:Solderpad_1x2, B.Cu at (127.8, 103.5)
- added J6: Conn_01x01_Pin, Bergi:Solderpad_1x2, B.Cu at (166.2, 84.3)
- added J6: Conn_01x01_Pin, Bergi:Solderpad_1x2, B.Cu at (89.3, 46.0)
- added J6: Conn_01x01_Pin, Bergi:Solderpad_1x2, B.Cu at (108.5, 84.3)
- added J6: Conn_01x01_Pin, Bergi:Solderpad_1x2, B.Cu at (108.5, 46.0)
- added J6: Conn_01x01_Pin, Bergi:Solderpad_1x2, B.Cu at (89.3, 65.2)
- added J6: Conn_01x01_Pin, Bergi:Solderpad_1x2, B.Cu at (146.9, 65.2)
- added J6: Conn_01x01_Pin, Bergi:Solderpad_1x2, B.Cu at (108.5, 65.2)
- added J6: Conn_01x01_Pin, Bergi:Solderpad_1x2, B.Cu at (146.9, 103.5)
- added J6: Conn_01x01_Pin, Bergi:Solderpad_1x2, B.Cu at (127.8, 84.3)
- added J6: Conn_01x01_Pin, Bergi:Solderpad_1x2, B.Cu at (146.9, 46.0)
- added J6: Conn_01x01_Pin, Bergi:Solderpad_1x2, B.Cu at (127.8, 122.8)
- added J6: Conn_01x01_Pin, Bergi:Solderpad_1x2, B.Cu at (166.2, 46.0)
- added J6: Conn_01x01_Pin, Bergi:Solderpad_1x2, B.Cu at (146.9, 122.8)
- added J6: Conn_01x01_Pin, Bergi:Solderpad_1x2, B.Cu at (89.3, 84.3)
- added J6: Conn_01x01_Pin, Bergi:Solderpad_1x2, B.Cu at (89.3, 103.5)
- added J6: Conn_01x01_Pin, Bergi:Solderpad_1x2, B.Cu at (108.5, 103.5)
- added J6: Conn_01x01_Pin, Bergi:Solderpad_1x2, B.Cu at (166.2, 65.2)
- added J6: Conn_01x01_Pin, Bergi:Solderpad_1x2, B.Cu at (146.9, 84.3)
- added J6: Conn_01x01_Pin, Bergi:Solderpad_1x2, B.Cu at (108.5, 122.8)
- added J6: Conn_01x01_Pin, Bergi:Solderpad_1x2, B.Cu at (166.2, 103.5)
- added J6: Conn_01x01_Pin, Bergi:Solderpad_1x2, B.Cu at (166.2, 122.8)
- added J6: Conn_01x01_Pin, Bergi:Solderpad_1x2, B.Cu at (127.8, 46.0)
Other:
- board text added: "PogoPcb V1.0"
